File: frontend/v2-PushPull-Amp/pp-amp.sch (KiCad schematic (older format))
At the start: 72 parts, among them K1 HK4100, P1 Antenna, P2 CONN_02X07, P3 TX Power Tap, P4 TX-IN, P5 RX IN, P6 12-13.8v, Q1 PZT2222A, Q2 RD16HHF1, T1 OUT_TRANSF, T2 BN-43-2402, U1 LP2951-50D

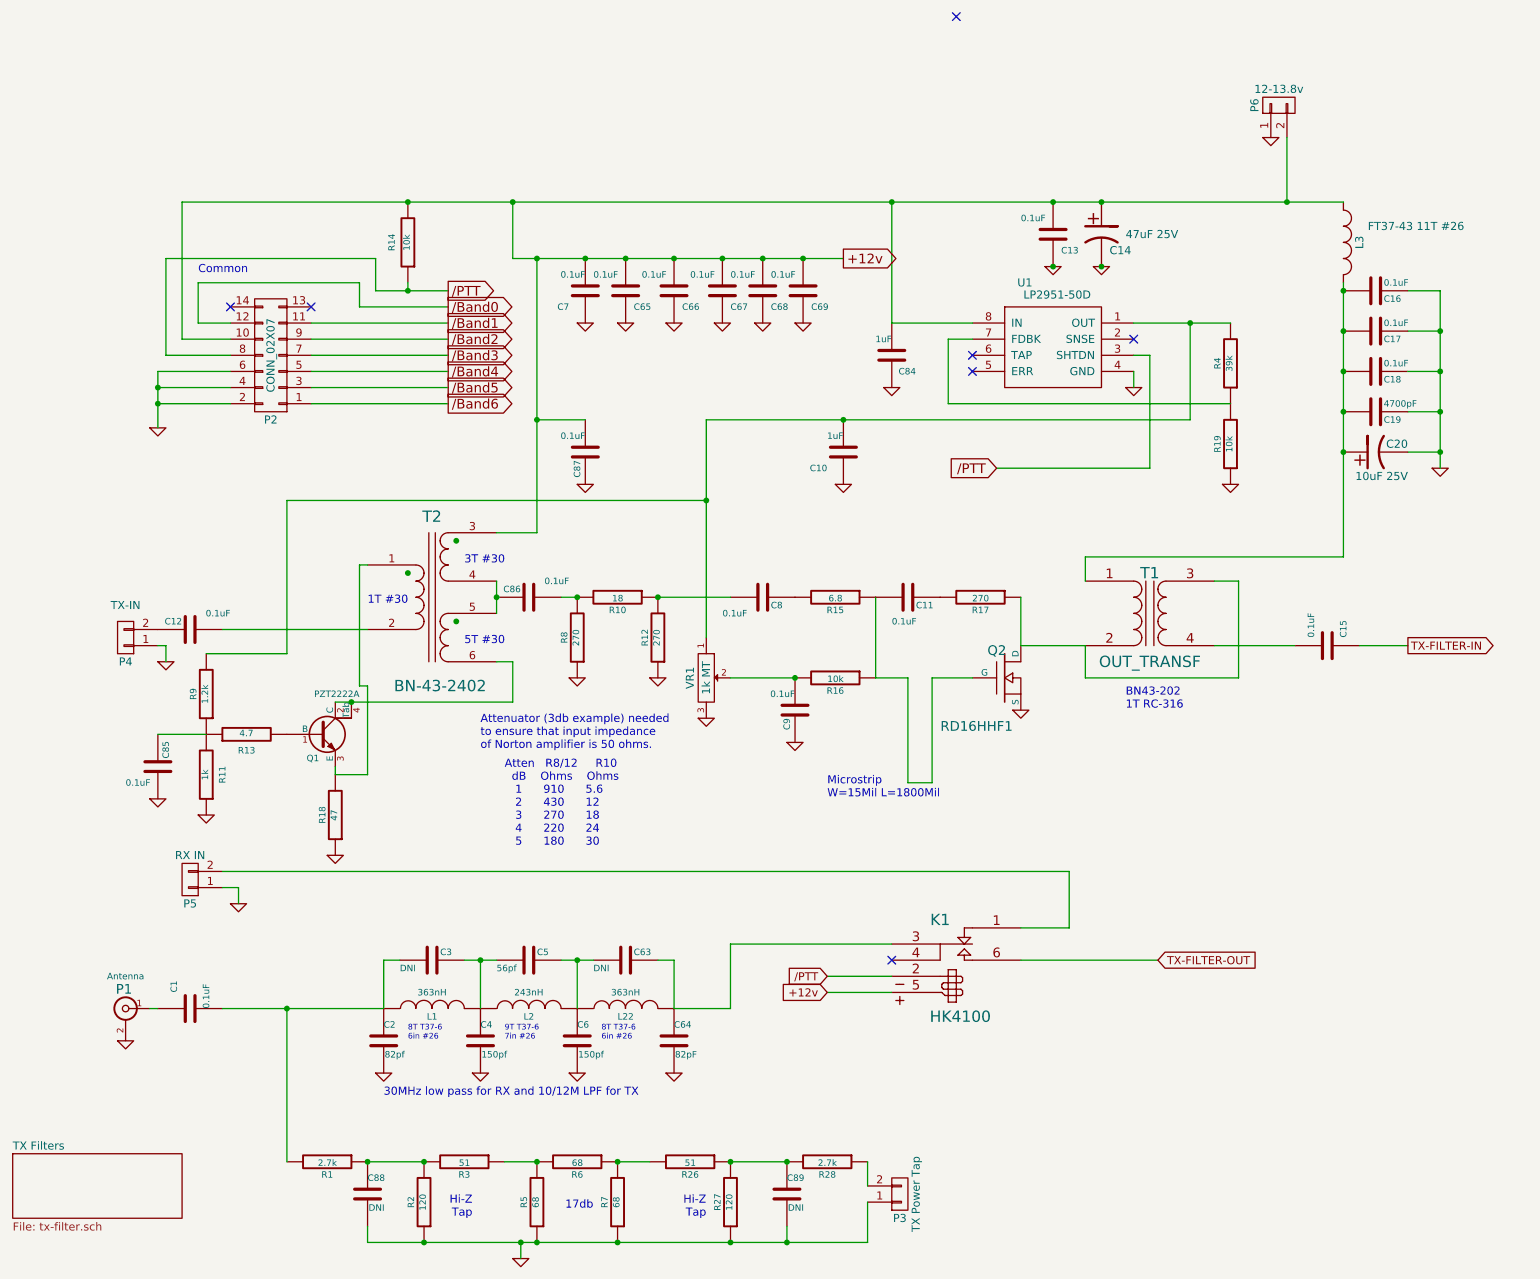
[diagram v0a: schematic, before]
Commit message: Went back to using input transformer with 50R unbalanced input
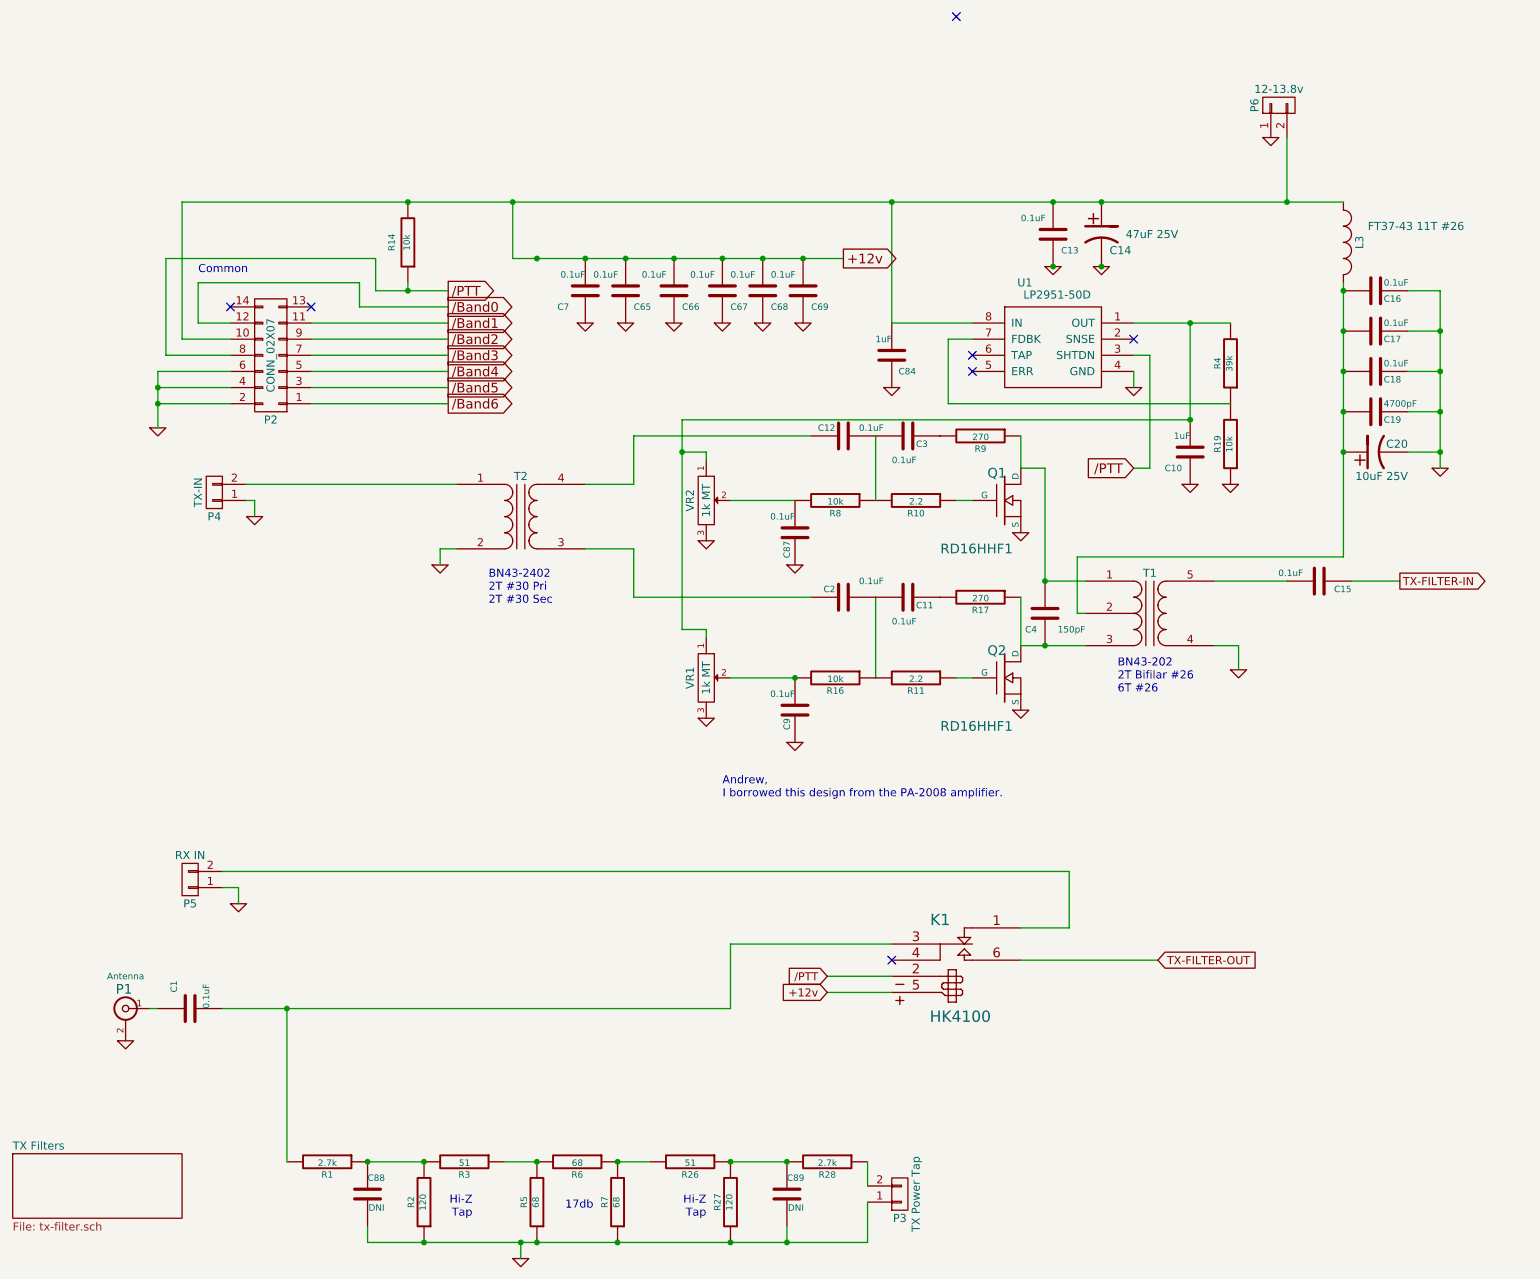
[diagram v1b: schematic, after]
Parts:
- removed C5: 56pf, HERMESLITE:C_0805, symbol C-RESCUE-amp
- removed C6: 150pf, HERMESLITE:C_0805, symbol C-RESCUE-amp
- removed C63: DNI, HERMESLITE:C_0805, symbol C-RESCUE-amp
- removed C64: 82pF, HERMESLITE:C_0805, symbol C-RESCUE-amp
- removed C8, C85, C86: 0.1uF, HERMESLITE:C_0805, symbol C-RESCUE-amp
- removed L1, L22: 363nH, HERMESLITE:Choke_Toroid, symbol INDUCTOR
- removed L2: 243nH, HERMESLITE:Choke_Toroid, symbol INDUCTOR
- removed Q1: PZT2222A, TO_SOT_Packages_SMD:SOT-223, symbol PZT2222A-T
- removed R12: 270, Resistors_SMD:R_0805_HandSoldering, symbol R-RESCUE-amp
- removed R13: 4.7, Resistors_SMD:R_0805_HandSoldering, symbol R-RESCUE-amp
- removed R15: 6.8, Resistors_SMD:R_0805_HandSoldering, symbol R-RESCUE-amp
- removed R18: 47, Resistors_SMD:R_0805_HandSoldering, symbol R-RESCUE-amp
- removed T1: OUT_TRANSF, HERMESLITE:OUT_TRANSF, symbol OUT_TRANSF
- removed T2: BN-43-2402, HERMESLITE:TRANSF, symbol TRANSFO2
- added Q1: RD16HHF1, TO_SOT_Packages_THT:TO-220_Neutral123_Vertical, symbol RD16HHF1
- added T1: TRANSFO4, HERMESLITE:OUT_TRANSF_PP, symbol TRANSFO4
- added T2: TRANSFO, Pin_Headers:Pin_Header_Straight_2x02, symbol TRANSFO
- added VR2: 1k MT, Potentiometers:Potentiometer_Bourns_3296W_3-8Zoll_Inline_ScrewUp, symbol POT
- C2: value 82pf -> 0.1uF
- C3: value DNI -> 0.1uF
- C4: value 150pf -> 150pF; footprint HERMESLITE:C_0805 -> Capacitors_ThroughHole:C_Rect_L7_W2_P5
- Q2: footprint Transistors_TO-220:TO-220_Neutral123_Vertical -> TO_SOT_Packages_THT:TO-220_Neutral123_Vertical
- R10: value 18 -> 2.2
- R11: value 1k -> 2.2
- R8: value 270 -> 10k
- R9: value 1.2k -> 270
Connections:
- net +12v: no longer C87.2
- net GND: now also Q1.2 (S), T1.4 (S1), T2.2 (AB), VR2.3; no longer C2.2, C4.2, R11.1, R8.1
- net at R10.1: now also Q1.1 (G)
- net at C11.2, R16.1: now also C2.2, R11.2; no longer Q2.1 (G)
- net at Q2.3 (D), R17.1: now also C4.1, T1.3 (PR2)
- net at C10.2, R4.2, U1.1 (OUT)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: now also VR2.1; no longer R9.2
- net at C16.2, C17.2, C18.2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: now also T1.2 (PM)
- net at C15.1: now also T1.5 (S2)
- net at R10.2: now also C12.2, C3.2, R8.1; no longer R8.2
- net at C1.2, R1.2: now also K1.3; no longer C2.1, C3.2
- net at C12.1: now also T2.4 (SB); no longer P4.2 (P2)
- net at R9.1: now also C4.2, Q1.3 (D), T1.1 (PR1); no longer R11.2
- net at C3.1: now also R9.2; no longer C4.1
- new net: Q2.1 (G), R11.1
- new net: C87.2, R8.2, VR2.2
- new net: C2.1, T2.3 (SA)
- new net: P4.2 (P2), T2.1 (AA)
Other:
- note added: "Andrew,\nI borrowed this design from the PA-2008 amplifier."
- note added: "BN43-202\n2T Bifilar #26\n6T #26"
- note added: "BN43-2402\n2T #30 Pri\n2T #30 Sec"
- note removed: "1T #30\n"
- note removed: "30MHz low pass for RX and 10/12M LPF for TX"
- note removed: "3T #30\n"
- note removed: "5T #30\n"
- note removed: "8T T37-6\n6in #26"
- note removed: "9T T37-6\n7in #26"
- note removed: "Atten R8/12 R10\n dB Ohms Ohms\n 1 910 5.6\n 2 430 12\n 3 270 18\n 4 220 24\n 5 180 30"
- note removed: "Attenuator (3db example) needed \nto ensure that input impedance\nof Norton amplifier is 50 ohms."
- note removed: "BN43-202\n1T RC-316"
- note removed: "Microstrip\nW=15Mil L=1800Mil"
- moved on the sheet: C10, C12, C15
